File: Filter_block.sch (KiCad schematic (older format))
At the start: 6 parts

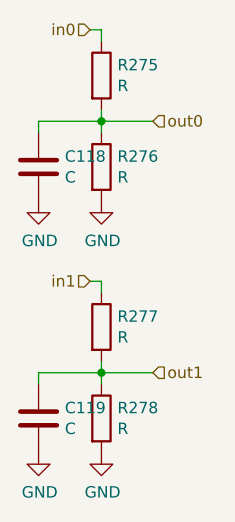
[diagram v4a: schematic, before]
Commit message: Eletrical Rules Check
Fixed some label names
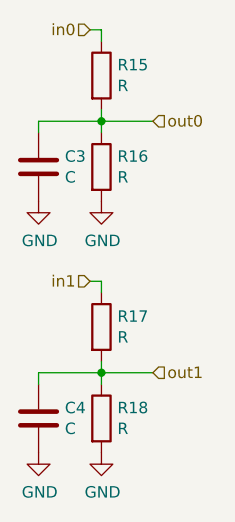
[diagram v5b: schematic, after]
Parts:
- renumbered C102 to C3, C103 to C4, R243 to R15, R244 to R16, R245 to R17, R246 to R18
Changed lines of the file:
@@
 AR Path="/596D7A67/5BE230A7/5BE230D0" Ref="R?"  Part="1"
 AR Path="/596D7A67/5BE80466/5BE230D0" Ref="R?"  Part="1"
-AR Path="/596D7A67/5C1804A3/5C1981DB/5BE230D0" Ref="R243"  Part="1"
-AR Path="/596D7A67/5C1804A3/5C19820B/5BE230D0" Ref="R259"  Part="1"
-AR Path="/596D7A67/5C1804A3/5C1BC561/5BE230D0" Ref="R275"  Part="1"
-AR Path="/5E49E893/5E67E090/5BE230D0" Ref="R275"  Part="1"
-F 0 "R275" H 2920 1696 50  0000 L CNN
+AR Path="/596D7A67/5C1804A3/5C1981DB/5BE230D0" Ref="R?"  Part="1"
+AR Path="/596D7A67/5C1804A3/5C19820B/5BE230D0" Ref="R?"  Part="1"
+AR Path="/596D7A67/5C1804A3/5C1BC561/5BE230D0" Ref="R?"  Part="1"
+AR Path="/5E49E893/5E67E090/5BE230D0" Ref="R15"  Part="1"
+F 0 "R15" H 2920 1696 50  0000 L CNN
 F 1 "R" H 2920 1605 50  0000 L CNN
 F 2 "Resistors_SMD:R_0603" V 2780 1650 50  0001 C CNN
@@
 AR Path="/596D7A67/5BE230A7/5BE23186" Ref="R?"  Part="1"
 AR Path="/596D7A67/5BE80466/5BE23186" Ref="R?"  Part="1"
-AR Path="/596D7A67/5C1804A3/5C1981DB/5BE23186" Ref="R244"  Part="1"
-AR Path="/596D7A67/5C1804A3/5C19820B/5BE23186" Ref="R260"  Part="1"
-AR Path="/596D7A67/5C1804A3/5C1BC561/5BE23186" Ref="R276"  Part="1"
-AR Path="/5E49E893/5E67E090/5BE23186" Ref="R276"  Part="1"
-F 0 "R276" H 2920 2096 50  0000 L CNN
+AR Path="/596D7A67/5C1804A3/5C1981DB/5BE23186" Ref="R?"  Part="1"
+AR Path="/596D7A67/5C1804A3/5C19820B/5BE23186" Ref="R?"  Part="1"
+AR Path="/596D7A67/5C1804A3/5C1BC561/5BE23186" Ref="R?"  Part="1"
+AR Path="/5E49E893/5E67E090/5BE23186" Ref="R16"  Part="1"
+F 0 "R16" H 2920 2096 50  0000 L CNN
 F 1 "R" H 2920 2005 50  0000 L CNN
 F 2 "Resistors_SMD:R_0603" V 2780 2050 50  0001 C CNN
@@
 AR Path="/596D7A67/5BE230A7/5BE231FF" Ref="C?"  Part="1"
 AR Path="/596D7A67/5BE80466/5BE231FF" Ref="C?"  Part="1"
-AR Path="/596D7A67/5C1804A3/5C1981DB/5BE231FF" Ref="C102"  Part="1"
-AR Path="/596D7A67/5C1804A3/5C19820B/5BE231FF" Ref="C110"  Part="1"
-AR Path="/596D7A67/5C1804A3/5C1BC561/5BE231FF" Ref="C118"  Part="1"
-AR Path="/5E49E893/5E67E090/5BE231FF" Ref="C118"  Part="1"
-F 0 "C118" H 2690 2096 50  0000 L CNN
+AR Path="/596D7A67/5C1804A3/5C1981DB/5BE231FF" Ref="C?"  Part="1"
+AR Path="/596D7A67/5C1804A3/5C19820B/5BE231FF" Ref="C?"  Part="1"
+AR Path="/596D7A67/5C1804A3/5C1BC561/5BE231FF" Ref="C?"  Part="1"
+AR Path="/5E49E893/5E67E090/5BE231FF" Ref="C3"  Part="1"
+F 0 "C3" H 2690 2096 50  0000 L CNN
 F 1 "C" H 2690 2005 50  0000 L CNN
 F 2 "Capacitors_SMD:C_0603" H 2613 1900 50  0001 C CNN
@@
 AR Path="/596D7A67/5BE230A7/5BE232A5" Ref="#PWR?"  Part="1"
 AR Path="/596D7A67/5BE80466/5BE232A5" Ref="#PWR?"  Part="1"
-AR Path="/596D7A67/5C1804A3/5C1981DB/5BE232A5" Ref="#PWR0522"  Part="1"
-AR Path="/596D7A67/5C1804A3/5C19820B/5BE232A5" Ref="#PWR0538"  Part="1"
-AR Path="/596D7A67/5C1804A3/5C1BC561/5BE232A5" Ref="#PWR0554"  Part="1"
-AR Path="/5E49E893/5E67E090/5BE232A5" Ref="#PWR0554"  Part="1"
-F 0 "#PWR0554" H 2850 1950 50  0001 C CNN
+AR Path="/596D7A67/5C1804A3/5C1981DB/5BE232A5" Ref="#PWR?"  Part="1"
+AR Path="/596D7A67/5C1804A3/5C19820B/5BE232A5" Ref="#PWR?"  Part="1"
+AR Path="/596D7A67/5C1804A3/5C1BC561/5BE232A5" Ref="#PWR?"  Part="1"
+AR Path="/5E49E893/5E67E090/5BE232A5" Ref="#PWR032"  Part="1"
+F 0 "#PWR032" H 2850 1950 50  0001 C CNN
 F 1 "GND" H 2855 2027 50  0000 C CNN
 F 2 "" H 2850 2200 50  0001 C CNN
@@
 AR Path="/596D7A67/5BE230A7/5BE2328D" Ref="#PWR?"  Part="1"
 AR Path="/596D7A67/5BE80466/5BE2328D" Ref="#PWR?"  Part="1"
-AR Path="/596D7A67/5C1804A3/5C1981DB/5BE2328D" Ref="#PWR0518"  Part="1"
-AR Path="/596D7A67/5C1804A3/5C19820B/5BE2328D" Ref="#PWR0534"  Part="1"
-AR Path="/596D7A67/5C1804A3/5C1BC561/5BE2328D" Ref="#PWR0550"  Part="1"
-AR Path="/5E49E893/5E67E090/5BE2328D" Ref="#PWR0550"  Part="1"
-F 0 "#PWR0550" H 2575 1950 50  0001 C CNN
+AR Path="/596D7A67/5C1804A3/5C1981DB/5BE2328D" Ref="#PWR?"  Part="1"
+AR Path="/596D7A67/5C1804A3/5C19820B/5BE2328D" Ref="#PWR?"  Part="1"
+AR Path="/596D7A67/5C1804A3/5C1BC561/5BE2328D" Ref="#PWR?"  Part="1"
+AR Path="/5E49E893/5E67E090/5BE2328D" Ref="#PWR030"  Part="1"
+F 0 "#PWR030" H 2575 1950 50  0001 C CNN
 F 1 "GND" H 2580 2027 50  0000 C CNN
 F 2 "" H 2575 2200 50  0001 C CNN
@@
 AR Path="/596D7A67/5BE230A7/5BE25BE7" Ref="R?"  Part="1"
 AR Path="/596D7A67/5BE80466/5BE25BE7" Ref="R?"  Part="1"
-AR Path="/596D7A67/5C1804A3/5C1981DB/5BE25BE7" Ref="R245"  Part="1"
-AR Path="/596D7A67/5C1804A3/5C19820B/5BE25BE7" Ref="R261"  Part="1"
-AR Path="/596D7A67/5C1804A3/5C1BC561/5BE25BE7" Ref="R277"  Part="1"
-AR Path="/5E49E893/5E67E090/5BE25BE7" Ref="R277"  Part="1"
-F 0 "R277" H 2920 2796 50  0000 L CNN
+AR Path="/596D7A67/5C1804A3/5C1981DB/5BE25BE7" Ref="R?"  Part="1"
+AR Path="/596D7A67/5C1804A3/5C19820B/5BE25BE7" Ref="R?"  Part="1"
+AR Path="/596D7A67/5C1804A3/5C1BC561/5BE25BE7" Ref="R?"  Part="1"
+AR Path="/5E49E893/5E67E090/5BE25BE7" Ref="R17"  Part="1"
+F 0 "R17" H 2920 2796 50  0000 L CNN
 F 1 "R" H 2920 2705 50  0000 L CNN
 F 2 "Resistors_SMD:R_0603" V 2780 2750 50  0001 C CNN
@@
 AR Path="/596D7A67/5BE230A7/5BE25BEE" Ref="R?"  Part="1"
 AR Path="/596D7A67/5BE80466/5BE25BEE" Ref="R?"  Part="1"
-AR Path="/596D7A67/5C1804A3/5C1981DB/5BE25BEE" Ref="R246"  Part="1"
-AR Path="/596D7A67/5C1804A3/5C19820B/5BE25BEE" Ref="R262"  Part="1"
-AR Path="/596D7A67/5C1804A3/5C1BC561/5BE25BEE" Ref="R278"  Part="1"
-AR Path="/5E49E893/5E67E090/5BE25BEE" Ref="R278"  Part="1"
-F 0 "R278" H 2920 3196 50  0000 L CNN
+AR Path="/596D7A67/5C1804A3/5C1981DB/5BE25BEE" Ref="R?"  Part="1"
+AR Path="/596D7A67/5C1804A3/5C19820B/5BE25BEE" Ref="R?"  Part="1"
+AR Path="/596D7A67/5C1804A3/5C1BC561/5BE25BEE" Ref="R?"  Part="1"
+AR Path="/5E49E893/5E67E090/5BE25BEE" Ref="R18"  Part="1"
+F 0 "R18" H 2920 3196 50  0000 L CNN
 F 1 "R" H 2920 3105 50  0000 L CNN
 F 2 "Resistors_SMD:R_0603" V 2780 3150 50  0001 C CNN
@@
 AR Path="/596D7A67/5BE230A7/5BE25BF5" Ref="C?"  Part="1"
 AR Path="/596D7A67/5BE80466/5BE25BF5" Ref="C?"  Part="1"
-AR Path="/596D7A67/5C1804A3/5C1981DB/5BE25BF5" Ref="C103"  Part="1"
-AR Path="/596D7A67/5C1804A3/5C19820B/5BE25BF5" Ref="C111"  Part="1"
-AR Path="/596D7A67/5C1804A3/5C1BC561/5BE25BF5" Ref="C119"  Part="1"
-AR Path="/5E49E893/5E67E090/5BE25BF5" Ref="C119"  Part="1"
-F 0 "C119" H 2690 3196 50  0000 L CNN
+AR Path="/596D7A67/5C1804A3/5C1981DB/5BE25BF5" Ref="C?"  Part="1"
+AR Path="/596D7A67/5C1804A3/5C19820B/5BE25BF5" Ref="C?"  Part="1"
+AR Path="/596D7A67/5C1804A3/5C1BC561/5BE25BF5" Ref="C?"  Part="1"
+AR Path="/5E49E893/5E67E090/5BE25BF5" Ref="C4"  Part="1"
+F 0 "C4" H 2690 3196 50  0000 L CNN
 F 1 "C" H 2690 3105 50  0000 L CNN
 F 2 "Capacitors_SMD:C_0603" H 2613 3000 50  0001 C CNN
@@
 AR Path="/596D7A67/5BE230A7/5BE25C06" Ref="#PWR?"  Part="1"
 AR Path="/596D7A67/5BE80466/5BE25C06" Ref="#PWR?"  Part="1"
-AR Path="/596D7A67/5C1804A3/5C1981DB/5BE25C06" Ref="#PWR0523"  Part="1"
-AR Path="/596D7A67/5C1804A3/5C19820B/5BE25C06" Ref="#PWR0539"  Part="1"
-AR Path="/596D7A67/5C1804A3/5C1BC561/5BE25C06" Ref="#PWR0555"  Part="1"
-AR Path="/5E49E893/5E67E090/5BE25C06" Ref="#PWR0555"  Part="1"
-F 0 "#PWR0555" H 2850 3050 50  0001 C CNN
+AR Path="/596D7A67/5C1804A3/5C1981DB/5BE25C06" Ref="#PWR?"  Part="1"
+AR Path="/596D7A67/5C1804A3/5C19820B/5BE25C06" Ref="#PWR?"  Part="1"
+AR Path="/596D7A67/5C1804A3/5C1BC561/5BE25C06" Ref="#PWR?"  Part="1"
+AR Path="/5E49E893/5E67E090/5BE25C06" Ref="#PWR033"  Part="1"
+F 0 "#PWR033" H 2850 3050 50  0001 C CNN
 F 1 "GND" H 2855 3127 50  0000 C CNN
 F 2 "" H 2850 3300 50  0001 C CNN
@@
 AR Path="/596D7A67/5BE230A7/5BE25C0C" Ref="#PWR?"  Part="1"
 AR Path="/596D7A67/5BE80466/5BE25C0C" Ref="#PWR?"  Part="1"
-AR Path="/596D7A67/5C1804A3/5C1981DB/5BE25C0C" Ref="#PWR0519"  Part="1"
-AR Path="/596D7A67/5C1804A3/5C19820B/5BE25C0C" Ref="#PWR0535"  Part="1"
-AR Path="/596D7A67/5C1804A3/5C1BC561/5BE25C0C" Ref="#PWR0551"  Part="1"
-AR Path="/5E49E893/5E67E090/5BE25C0C" Ref="#PWR0551"  Part="1"
-F 0 "#PWR0551" H 2575 3050 50  0001 C CNN
+AR Path="/596D7A67/5C1804A3/5C1981DB/5BE25C0C" Ref="#PWR?"  Part="1"
+AR Path="/596D7A67/5C1804A3/5C19820B/5BE25C0C" Ref="#PWR?"  Part="1"
+AR Path="/596D7A67/5C1804A3/5C1BC561/5BE25C0C" Ref="#PWR?"  Part="1"
+AR Path="/5E49E893/5E67E090/5BE25C0C" Ref="#PWR031"  Part="1"
+F 0 "#PWR031" H 2575 3050 50  0001 C CNN
 F 1 "GND" H 2580 3127 50  0000 C CNN
 F 2 "" H 2575 3300 50  0001 C CNN
